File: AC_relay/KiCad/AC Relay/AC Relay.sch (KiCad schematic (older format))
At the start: 17 parts, among them J1 Screw_Terminal_01x02, J2 Conn_01x06_Female, J3 Screw_Terminal_01x02, K1 1461492-2, Q1 FDN537N, SW1 SW_Push, U1 BU33SD5WG-TR, U2 ESP-12E, U3 HLK-PM01

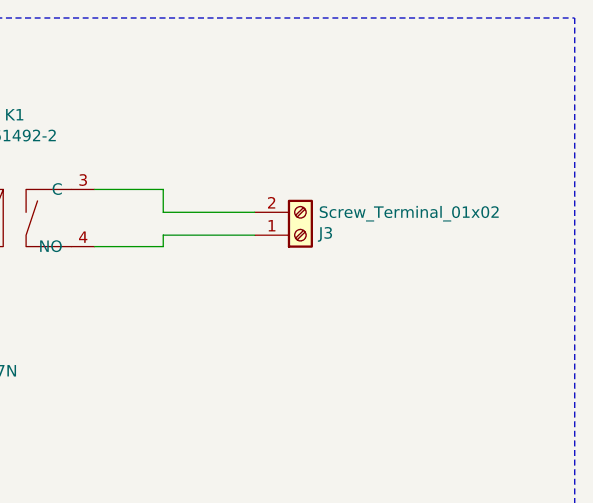
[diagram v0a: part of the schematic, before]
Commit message: Diode footprint fised
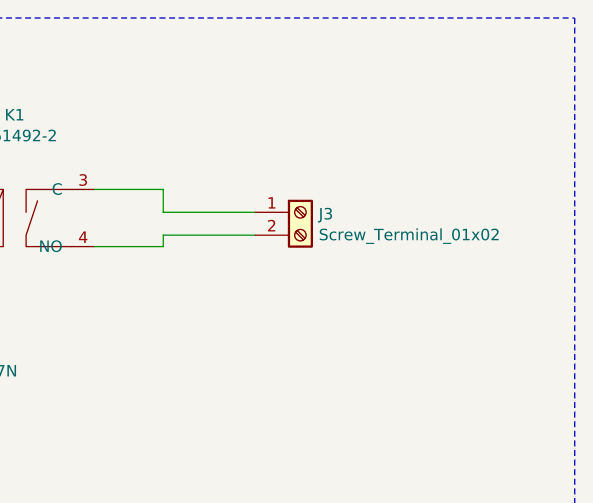
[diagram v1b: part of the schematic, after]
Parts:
- D1: footprint Diode_SMD:D_0201_0603Metric -> Diode_SMD:D_0603_1608Metric
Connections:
- net at K1.3 (C): now also J3.1 (Pin_1); no longer J3.2 (Pin_2)
- net at K1.4 (NO): now also J3.2 (Pin_2); no longer J3.1 (Pin_1)
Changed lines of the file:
@@
 F 0 "D1" V 6846 1922 50  0000 R CNN
 F 1 "RGF1B" V 6755 1922 50  0000 R CNN
-F 2 "Diode_SMD:D_0201_0603Metric" H 6800 2050 50  0001 C CNN
+F 2 "Diode_SMD:D_0603_1608Metric" H 6800 2050 50  0001 C CNN
 F 3 "https://www.mouser.es/datasheet/2/308/RGF1B-1301585.pdf" H 6800 2050 50  0001 C CNN
 	1    6800 2050
@@
 L Connector:Screw_Terminal_01x02 J3
 U 1 1 5C0B3318
-P 8700 2150
-F 0 "J3" H 8780 2142 50  0000 L CNN
-F 1 "Screw_Terminal_01x02" H 8780 2051 50  0000 L CNN
-F 2 "TerminalBlock:TerminalBlock_Altech_AK300-2_P5.00mm" H 8700 2150 50  0001 C CNN
-F 3 "https://www.mouser.es/datasheet/2/324/985920-1459071.pdf" H 8700 2150 50  0001 C CNN
-	1    8700 2150
-	1    0    0    1
+P 8700 2050
+F 0 "J3" H 8780 2042 50  0000 L CNN
+F 1 "Screw_Terminal_01x02" H 8780 1951 50  0000 L CNN
+F 2 "TerminalBlock:TerminalBlock_Altech_AK300-2_P5.00mm" H 8700 2050 50  0001 C CNN
+F 3 "https://www.mouser.es/datasheet/2/324/985920-1459071.pdf" H 8700 2050 50  0001 C CNN
+	1    8700 2050
+	1    0    0    -1
 $EndComp
 Wire Wire Line
@@
 	1    0    0    -1
 $EndComp
-Wire Wire Line
-	8100 2050 8500 2050
-Wire Wire Line
-	8500 2150 8100 2150
 $Comp
 L Device:Q_NMOS_GDSD Q1
@@
 Wire Wire Line
 	2200 4500 2950 4500
+Wire Wire Line
+	8100 2050 8500 2050
+Wire Wire Line
+	8500 2150 8100 2150
 $EndSCHEMATC
